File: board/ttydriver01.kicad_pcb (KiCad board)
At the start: 2 copper layers, 119.4 x 74.9 mm, 69 parts, among them J1 PRINTER JACK, J2 KEYBOARD JACK, J3 MOTOR CTL RELAY JACK, P1 CONN_01X02, SW1 Switch_SPDT, SW2 Button_SPDT, T1 Coilcraft-FA2469-AL, U1 NE555, U2 AP2553W6, U3 CP2102-breakout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

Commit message: Ready to go to fab
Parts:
- moved R15 1.27 mm to (106.4, 137.2)
- moved C4 0.52 mm to (127.4, 131.3)
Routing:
- net /HVNEG: track 135.0 -> 165.9 mm
- net Net-(C8-Pad1): track 63.3 -> 33.0 mm
- net GND: track 341.2 -> 367.7 mm
- net /OSC: track 39.7 -> 25.2 mm, vias 1 -> 2
- net Net-(C13-Pad1): track 273.6 -> 286.4 mm
- net Net-(J3-PadT): track 131.5 -> 120.4 mm
- net /TxD: track 118.4 -> 128.3 mm
- net Net-(C3-Pad1): track 95.5 -> 86.0 mm
- net Net-(C6-Pad1): track 14.7 -> 20.3 mm
- net Net-(C10-Pad1): track 52.9 -> 47.4 mm
- net Net-(C11-Pad1): track 65.2 -> 61.0 mm
- net /HVPOS: track 28.9 -> 24.7 mm, vias 1 -> 0
- net Net-(R9-Pad1): track 107.2 -> 110.4 mm
- net Net-(J2-PadS): track 101.4 -> 98.5 mm
- net Net-(R6-Pad1): track 24.0 -> 21.5 mm, vias 2 -> 0
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
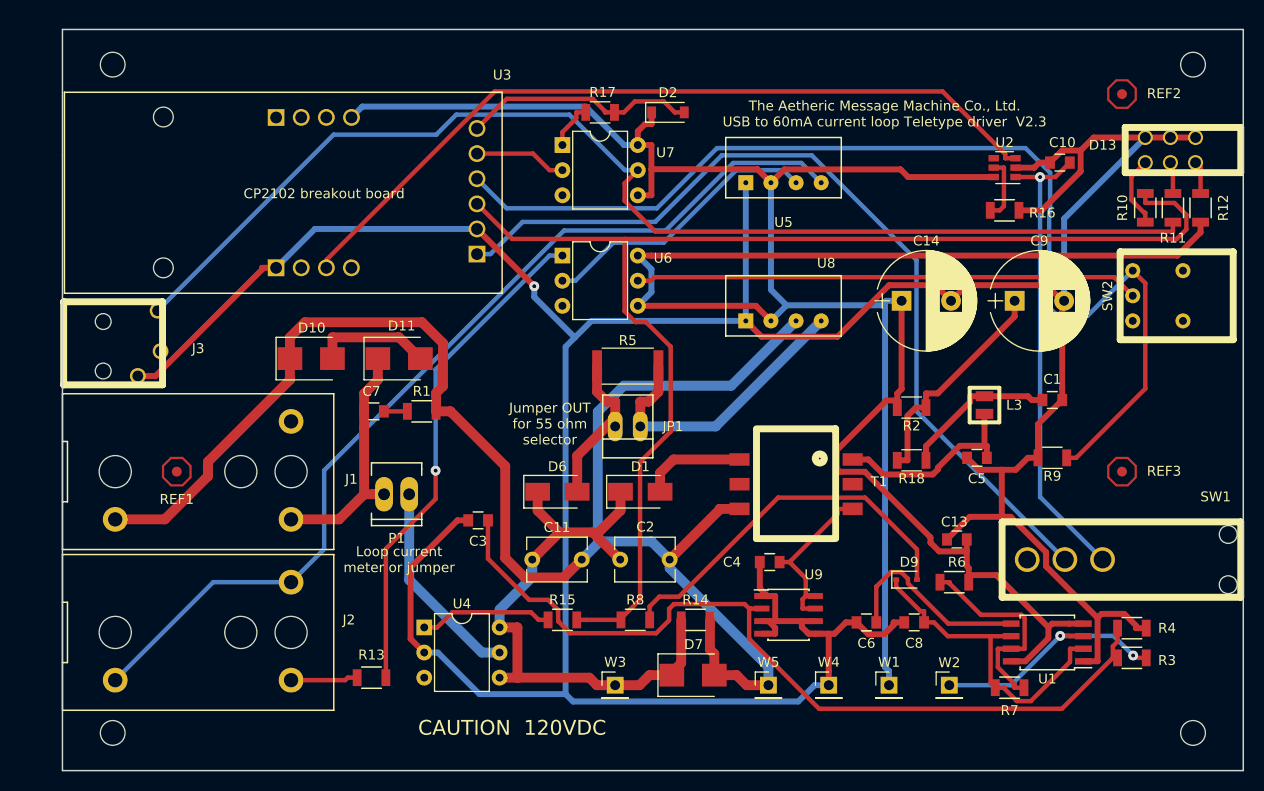
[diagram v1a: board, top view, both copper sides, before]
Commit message: Beginnings of layout. All components present
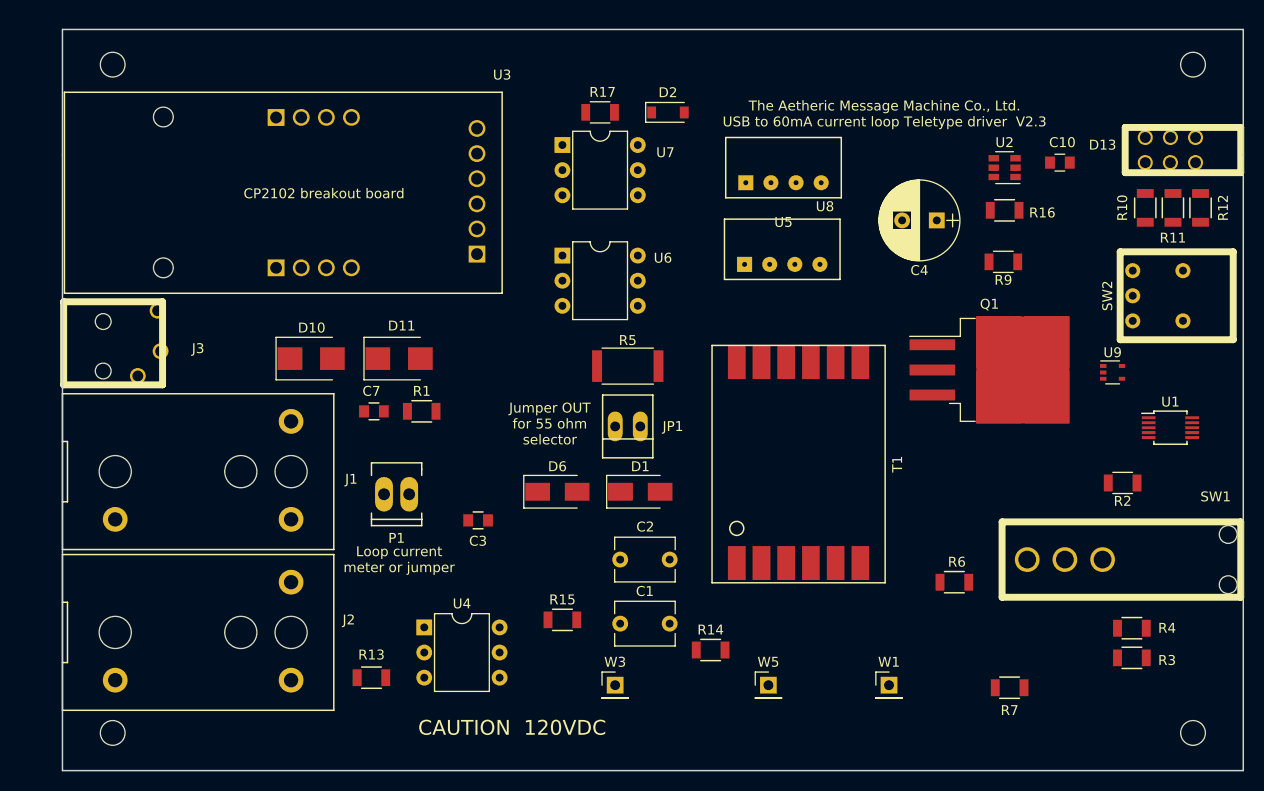
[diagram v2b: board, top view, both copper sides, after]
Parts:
- removed C11: 1uf, Capacitors_ThroughHole:C_Disc_D6.0mm_W4.4mm_P5.00mm
- removed C13, C5: 22uf, Capacitors_SMD:C_0805
- removed C14, C9: 470uf, Capacitors_ThroughHole:CP_Radial_D10.0mm_P5.00mm
- removed C6: 10nf, Capacitors_SMD:C_0805
- removed C8: 910pf, Capacitors_SMD:C_0805
- removed D7: 120V, Diodes_SMD:SMB_Standard
- removed D9: Schottky, Diodes_SMD:SOD-323
- removed L3: 10uH, Coilcraft:0508PS
- removed R18: 2.2, Resistors_SMD:R_1206
- removed R8: 2.2K, Resistors_SMD:R_1206
- removed REF1, REF2, REF3: Fiducial_Image_Seeed, Fiducials_SEEED:Fiducial_Image_Seeed_Top
- removed W2, W4: TEST_1P, Pin_Headers:Pin_Header_Straight_1x01_Pitch2.54mm
- added Q1: IRL530NS, TO_SOT_Packages_SMD:TO-263-3_TabPin2, F.Cu at (149.6, 111.9)
- C1: value 22uf -> 1uf; footprint Capacitors_SMD:C_0805 -> Capacitors_ThroughHole:C_Disc_D6.0mm_W4.4mm_P5.00mm
- C3: value 10pf -> 100pf
- C4: value 1000pf -> 220uf; footprint Capacitors_SMD:C_0805 -> Capacitors_ThroughHole:CP_Radial_D8.0mm_P3.50mm
- R2: value 2.2 -> 100K
- R3: value 22 -> 100m
- R4: value 10K -> 23K
- R6: value 715 -> 43K
- R7: value 7.15K -> 2.49K
- T1: value Coilcraft-FA2469-AL -> Coilcraft-DA2032; footprint Coilcraft:Coilcraft-FA2469-AL -> Coilcraft:Coilcraft-DA2032-AL
- U1: value NE555 -> LT3750; footprint Housings_SOIC:SOIJ-8_5.3x5.3mm_Pitch1.27mm -> Housings_SSOP:MSOP-10_3x3mm_Pitch0.5mm
- U9: value FDS4559 -> 74HC1GU04; footprint Housings_SOIC:SOIC-8_3.9x4.9mm_Pitch1.27mm -> TO_SOT_Packages_SMD:SOT-353_SC-70-5
- moved C1 49.2 mm to (112.3, 137.5)
- moved U9 40.9 mm to (162.1, 112.1)
- moved C4 38.5 mm to (144.3, 96.8)
- moved U1 25.0 mm to (167.9, 117.7), turned to 0 degrees
- moved R2 22.7 mm to (163.1, 123.3)
- moved R9 20.4 mm to (151.0, 101.0)
- moved U8 5.72 mm to (128.7, 101.2)
- moved R14 3.41 mm to (121.4, 140.2)
- moved T1 2.05 mm to (130.3, 121.4), turned to 90 degrees
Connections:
- C1 pad 2: GND -> /HVNEG
- C2 pad 1: Net-(C11-Pad1) -> Net-(C1-Pad1)
- D1 pad 1: Net-(C11-Pad1) -> Net-(C1-Pad1)
- D2 pad 1: Net-(C13-Pad1) -> Net-(C4-Pad1)
- D6 pad 1: Net-(C11-Pad1) -> Net-(C1-Pad1)
- R12 pad 2: Net-(C13-Pad1) -> Net-(C4-Pad1)
- R14 pad 1: Net-(C11-Pad1) -> Net-(C1-Pad1)
- R2 pad 1: Net-(C9-Pad1) -> Net-(R2-Pad1)
- R2 pad 2: Net-(C13-Pad1) -> Net-(C4-Pad1)
- R3 pad 1: Net-(C3-Pad1) -> Net-(Q1-Pad2)
- R3 pad 2: /OSC -> GND
- R4 pad 1: Net-(C3-Pad1) -> Net-(Q1-Pad3)
- R4 pad 2: GND -> Net-(R4-Pad2)
- R6 pad 1: Net-(R6-Pad1) -> Net-(Q1-Pad3)
- R6 pad 2: Net-(C13-Pad1) -> Net-(R6-Pad2)
- R7 pad 1: Net-(R6-Pad1) -> Net-(C3-Pad1)
- R7 pad 2: Net-(C8-Pad1) -> GND
- T1 pad 1: Net-(C5-Pad1) -> /HVNEG
- T1 pad 3: Net-(C4-Pad1) -> Net-(Q1-Pad3)
- T1 pad 4: /HVNEG -> Net-(Q1-Pad3)
- T1 pad 5: (no net) -> Net-(Q1-Pad3)
- T1 pad 6: Net-(D1-Pad2) -> Net-(Q1-Pad3)
- U1 pad 1: GND -> Net-(C4-Pad1)
- U1 pad 2: Net-(C8-Pad1) -> Net-(R2-Pad1)
- U1 pad 3: /OSC -> Net-(U1-Pad3)
- U1 pad 4: Net-(C13-Pad1) -> Net-(C4-Pad1)
- U1 pad 5: Net-(C6-Pad1) -> GND
- U1 pad 6: Net-(C8-Pad1) -> Net-(Q1-Pad2)
- U1 pad 7: Net-(R6-Pad1) -> Net-(Q1-Pad1)
- U1 pad 8: Net-(C13-Pad1) -> Net-(R6-Pad2)
- U2 pad 6: Net-(C13-Pad1) -> Net-(C4-Pad1)
- U3 pad 2-4: Net-(C13-Pad1) -> Net-(C4-Pad1)
- U4 pad 4: Net-(C11-Pad1) -> Net-(C1-Pad1)
- U4 pad 6: Net-(C11-Pad1) -> Net-(C1-Pad1)
- U5 pad 2: Net-(C13-Pad1) -> Net-(C4-Pad1)
- U6 pad 4: Net-(C13-Pad1) -> Net-(C4-Pad1)
- U6 pad 6: Net-(C13-Pad1) -> Net-(C4-Pad1)
- U7 pad 4: Net-(C13-Pad1) -> Net-(C4-Pad1)
- U7 pad 6: Net-(C13-Pad1) -> Net-(C4-Pad1)
- U8 pad 2: Net-(C13-Pad1) -> Net-(C4-Pad1)
- U9 pad 1: GND -> (no net)
- U9 pad 2: Net-(C3-Pad1) -> /TxD
- U9 pad 4: GND -> Net-(U1-Pad3)
- U9 pad 5: GND -> Net-(C4-Pad1)
- W1 pad 1: Net-(C13-Pad1) -> Net-(C4-Pad1)
- W3 pad 1: Net-(C11-Pad1) -> Net-(C1-Pad1)
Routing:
- net GND: track 367.7 -> 0.00 mm, vias 1 -> 0
- net Net-(C13-Pad1): track 286.4 -> 0.00 mm
- net /HVNEG: track 165.9 -> 0.00 mm
- net /TxD: track 128.3 -> 0.00 mm
- net Net-(J3-PadT): track 120.4 -> 0.00 mm
- net Net-(R9-Pad1): track 110.4 -> 0.00 mm
- net Net-(J2-PadS): track 98.5 -> 0.00 mm
- net Net-(SW1-Pad2): track 89.5 -> 0.00 mm
- net Net-(C3-Pad1): track 86.0 -> 0.00 mm
- net /ENABLE: track 80.6 -> 0.00 mm
- net Net-(C11-Pad1): track 61.0 -> 0.00 mm
- net /RxD: track 51.0 -> 0.00 mm
- net Net-(R13-Pad2): track 50.8 -> 0.00 mm, vias 1 -> 0
- net Net-(C10-Pad1): track 47.4 -> 0.00 mm, vias 1 -> 0
- net Net-(D9-Pad2): track 38.2 -> 0.00 mm
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
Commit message: Add capcharger sim
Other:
- board text added: "The Aetheric Message Machine Co., Ltd. USB to 60mA current loop Teletype driver V3.0"
- board text removed: "The Aetheric Message Machine Co., Ltd. USB to 60mA current loop Teletype driver V2.3"
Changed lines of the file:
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@@
     (effects (font (size 1.5 1.5) (thickness 0.3)))
   )
-  (gr_text "The Aetheric Message Machine Co., Ltd.\nUSB to 60mA current loop Teletype driver  V2.3" (at 139 86) (layer F.SilkS)
+  (gr_text "The Aetheric Message Machine Co., Ltd.\nUSB to 60mA current loop Teletype driver  V3.0" (at 139 86) (layer F.SilkS)
     (effects (font (size 1 1) (thickness 0.25)))
   )

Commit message: Working on trace widths
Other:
- net class Default: clearance 0.28 -> 0.2
- rule trace_clearance: 0.28 -> 0.2
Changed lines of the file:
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@@
     (links 109)
     (no_connects 105)
-    (area 55.804999 77.394999 175.335001 152.475001)
+    (area 52.531429 76.251 193.291156 161.450001)
     (thickness 1.6)
     (drawings 12)
@@
   (setup
     (last_trace_width 0.45)
-    (trace_clearance 0.28)
+    (trace_clearance 0.2)
     (zone_clearance 0.6)
     (zone_45_only yes)
@@
   (net 38 "Net-(U1-Pad3)")
   (net_class Default "This is the default net class."
-    (clearance 0.28)
+    (clearance 0.2)
     (trace_width 0.45)
     (via_dia 1)

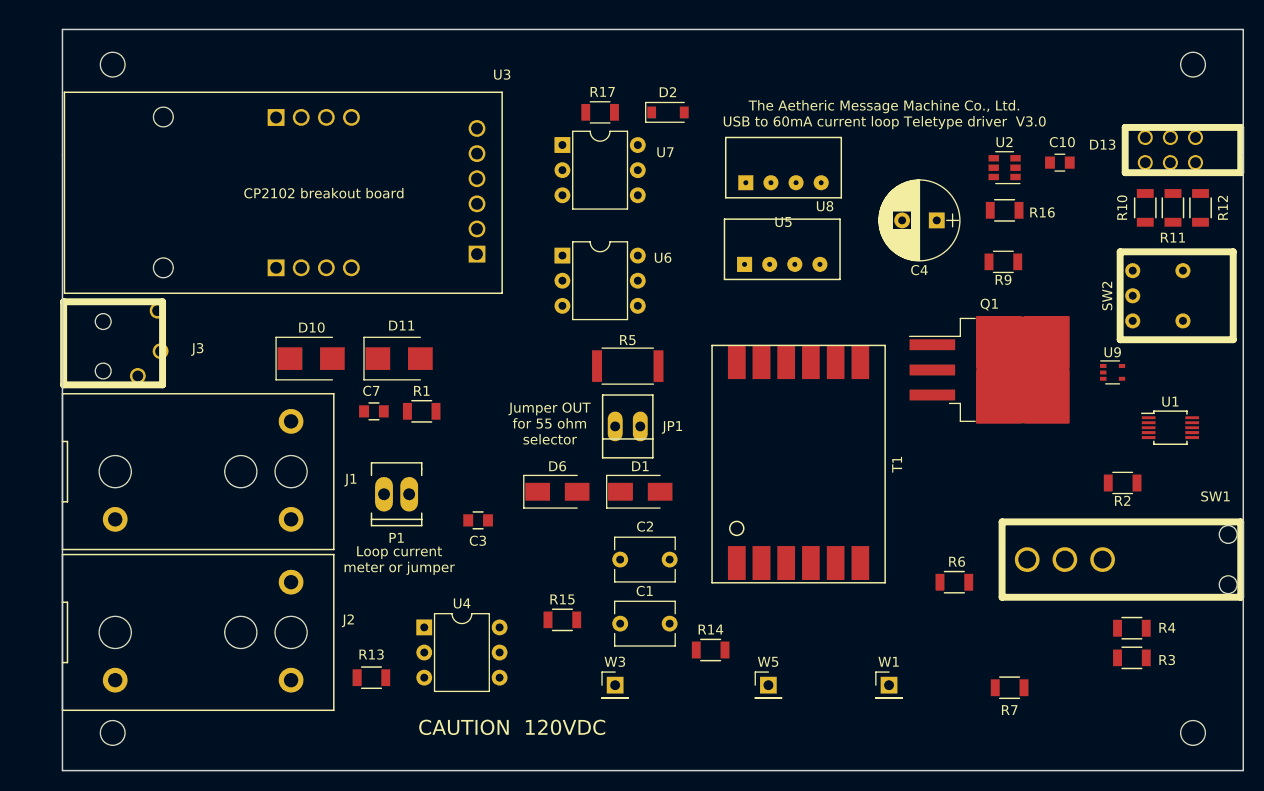
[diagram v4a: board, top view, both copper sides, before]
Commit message: Board passes DRC; corners clipped on layout
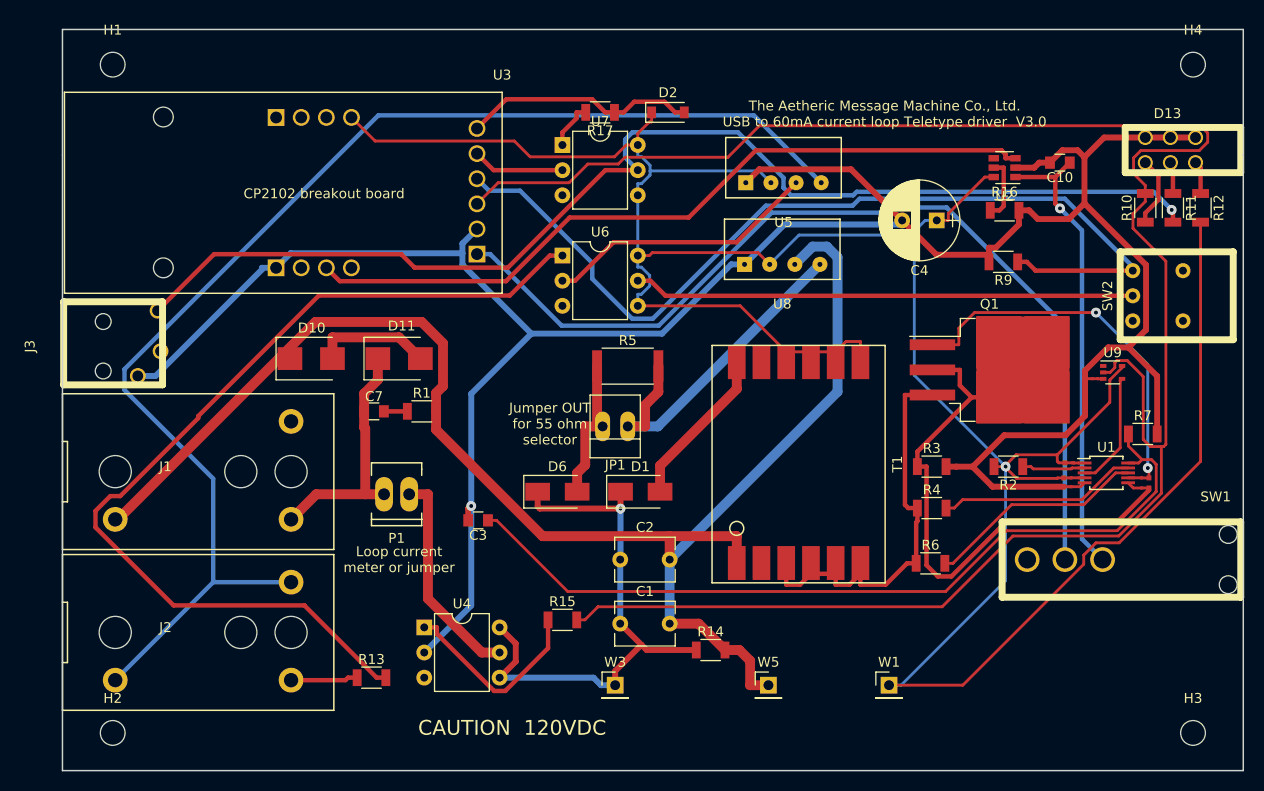
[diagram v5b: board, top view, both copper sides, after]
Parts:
- added M1: narrower_0.3mm, Utility:trace_narrower_0.3mm, F.Cu at (157.6, 123.7)
- added M2: narrower_0.3mm, Utility:trace_narrower_0.3mm, F.Cu at (165.2, 122.8)
- added M3: narrower_0.3mm, Utility:trace_narrower_0.3mm, F.Cu at (165.2, 123.8)
- added M4: narrower_0.3mm, Utility:trace_narrower_0.3mm, F.Cu at (157.7, 121.3)
- added M5: narrower_0.3mm, Utility:trace_narrower_0.3mm, F.Cu at (157.6, 122.8)
- added M7: narrower_0.3mm, Utility:trace_narrower_0.3mm, F.Cu at (159.8, 112.8)
- moved R7 29.0 mm to (165.1, 118.4), turned to 0 degrees
- moved R3 28.0 mm to (143.8, 121.7)
- moved R4 23.6 mm to (143.8, 125.9)
- moved R2 11.7 mm to (151.5, 121.7)
- moved U1 7.93 mm to (161.4, 122.3)
- moved R6 3.07 mm to (143.6, 131.4)
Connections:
- Q1 pad 1: Net-(Q1-Pad1) -> Net-(M2-Pad1)
- Q1 pad 2: Net-(Q1-Pad2) -> Net-(M3-Pad1)
- R3 pad 1: Net-(Q1-Pad2) -> Net-(M3-Pad1)
- U1 pad 1: Net-(C4-Pad1) -> Net-(M4-Pad2)
- U1 pad 4: Net-(C4-Pad1) -> Net-(M5-Pad2)
- U1 pad 5: GND -> Net-(M1-Pad2)
- U1 pad 6: Net-(Q1-Pad2) -> Net-(M3-Pad2)
- U1 pad 7: Net-(Q1-Pad1) -> Net-(M2-Pad2)
- U9 pad 3: GND -> Net-(M7-Pad2)
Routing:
- net Net-(C4-Pad1): track 0.00 -> 285.1 mm, vias 0 -> 1
- net GND: track 0.00 -> 264.7 mm, vias 0 -> 1
- net /TxD: track 0.00 -> 201.6 mm
- net /HVNEG: track 0.00 -> 156.0 mm
- net Net-(J2-PadS): track 0.00 -> 131.0 mm
- net Net-(J3-PadT): track 0.00 -> 120.2 mm, vias 0 -> 1
- net Net-(SW1-Pad2): track 0.00 -> 96.0 mm
- net Net-(R13-Pad2): track 0.00 -> 95.3 mm
- net Net-(R9-Pad1): track 0.00 -> 93.4 mm
- net Net-(C3-Pad1): track 0.00 -> 83.8 mm
- net /ENABLE: track 0.00 -> 76.3 mm
- net Net-(M3-Pad1): track 0.00 -> 71.8 mm
- net Net-(C1-Pad1): track 0.00 -> 55.7 mm, vias 0 -> 1
- net /RxD: track 0.00 -> 50.7 mm
- net Net-(C10-Pad1): track 0.00 -> 46.7 mm, vias 0 -> 1
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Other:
- net class Default: clearance 0.2 -> 0.25
- net class Thin added: clearance 0.2, trace_width 0.29, via_dia 1, via_drill 0.4
- rule trace_clearance: 0.2 -> 0.25

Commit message: Fix solder mask tolerance to avoid exposed copper at sharp corners
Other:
- rule pad_to_mask_clearance: 0.2 -> 0.15
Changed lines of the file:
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@@
     (pad_size 1.524 1.524)
     (pad_drill 0.762)
-    (pad_to_mask_clearance 0.2)
+    (pad_to_mask_clearance 0.15)
     (aux_axis_origin 0 0)
     (visible_elements FFFFFF7F)

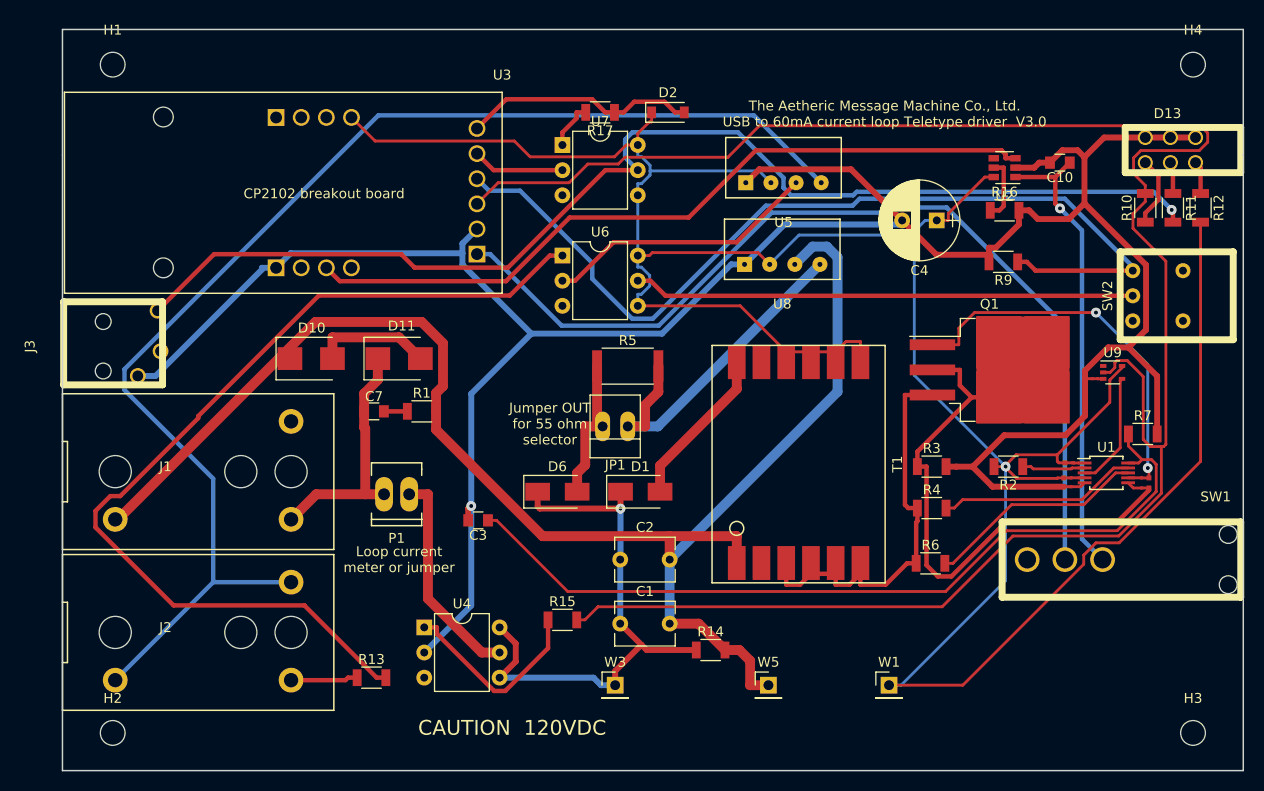
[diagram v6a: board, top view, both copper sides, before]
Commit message: 3D models fixed
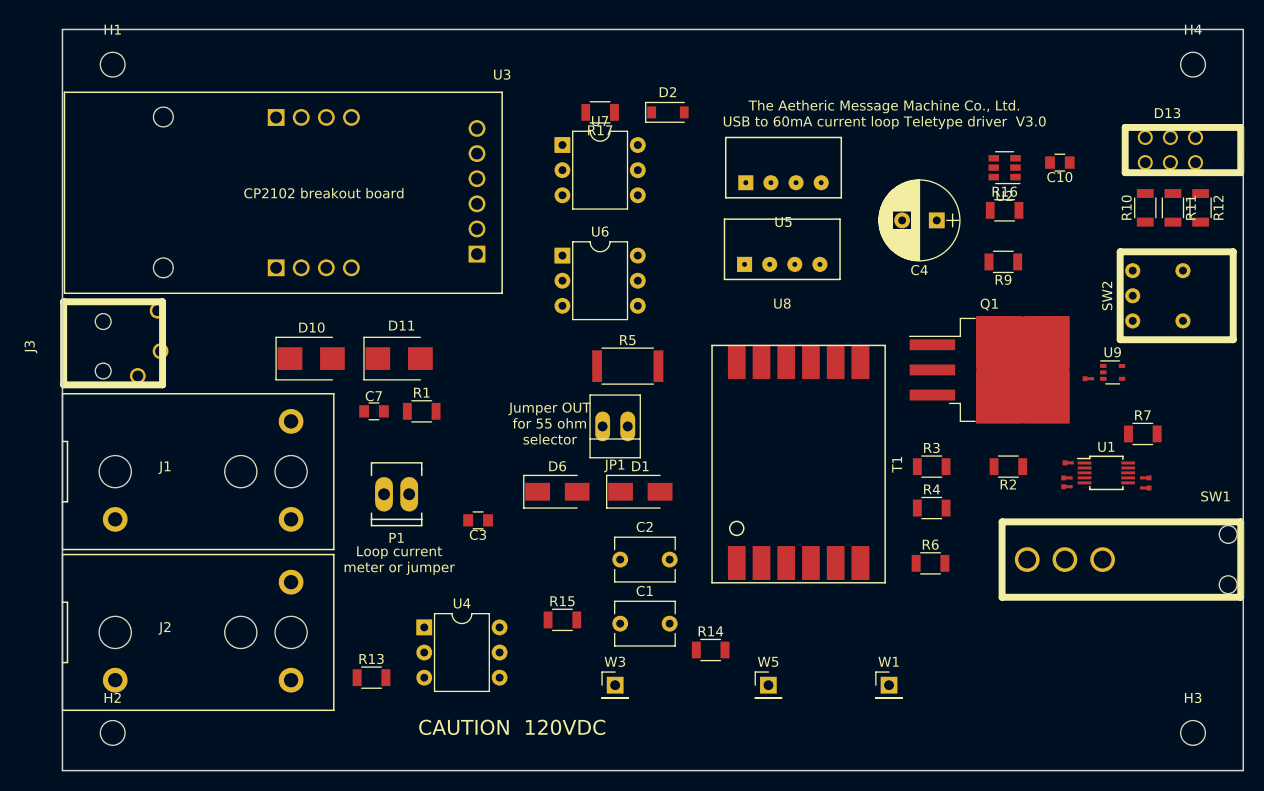
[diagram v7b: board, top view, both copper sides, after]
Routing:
- net Net-(C4-Pad1): track 285.1 -> 0.00 mm, vias 1 -> 0
- net GND: track 264.7 -> 0.00 mm, vias 1 -> 0
- net /TxD: track 201.6 -> 0.00 mm
- net /HVNEG: track 156.0 -> 0.00 mm
- net Net-(J2-PadS): track 131.0 -> 0.00 mm
- net Net-(J3-PadT): track 120.2 -> 0.00 mm, vias 1 -> 0
- net Net-(SW1-Pad2): track 96.0 -> 0.00 mm
- net Net-(R13-Pad2): track 95.3 -> 0.00 mm
- net Net-(R9-Pad1): track 93.4 -> 0.00 mm
- net Net-(C3-Pad1): track 83.8 -> 0.00 mm
- net /ENABLE: track 76.3 -> 0.00 mm
- net Net-(M3-Pad1): track 71.8 -> 0.00 mm
- net Net-(C1-Pad1): track 55.7 -> 0.00 mm, vias 1 -> 0
- net /RxD: track 50.7 -> 0.00 mm
- net Net-(C10-Pad1): track 46.7 -> 0.00 mm, vias 1 -> 0
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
